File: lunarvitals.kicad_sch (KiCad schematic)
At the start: 26 parts, among them J1 MLX90614, J2 MAX30102, J3 SEN11574, J4 ConductiveCord, U1 NRF52840-DONGLE, U2 BMP280, U3 AP2112K-3.3, U5 MPU-6050

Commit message: PCB layout
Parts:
- removed D2: Green_LED, LED_SMD:LED_0603_1608Metric, symbol Device:LED
- added R8: 4.7k, Resistor_SMD:R_0402_1005Metric, symbol Device:R
- J2: footprint Connector_PinSocket_2.00mm:PinSocket_2x02_P2.00mm_Vertical -> Connector_JST:JST_XA_B04B-XASK-1-A_1x04_P2.50mm_Vertical; symbol Connector_Generic:Conn_02x02_Odd_Even -> Connector_Generic:Conn_01x04; LCSC C46289 -> C491709
- J3, J4: footprint Connector_PinSocket_2.54mm:PinSocket_1x03_P2.54mm_Vertical -> Connector_JST:JST_XA_B03B-XASK-1-A_1x03_P2.50mm_Vertical; LCSC C146690 -> C265055
- R4: value 10k -> 4.7k; LCSC C25744 -> C25900
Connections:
- net +3.3V: now also J2.1 (Pin_1), R8.1; no longer J2.3 (Pin_3)
- net GND: now also J2.4 (Pin_4); no longer J2.1 (Pin_1)
- net I2C1_SCL: now also J2.3 (Pin_3); no longer J2.2 (Pin_2)
- net I2C1_SDA: now also J2.2 (Pin_2); no longer J2.4 (Pin_4)
- net at U5.6 (AUX_DA): now also R4.2
- net at U5.7 (AUX_CL): now also R8.2
- no-connect marks 4 -> 2
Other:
- note added: "LED On Indicator"
- note removed: "LED On Indicator (Red)"
- note removed: "On LED"
- moved on the sheet: J2

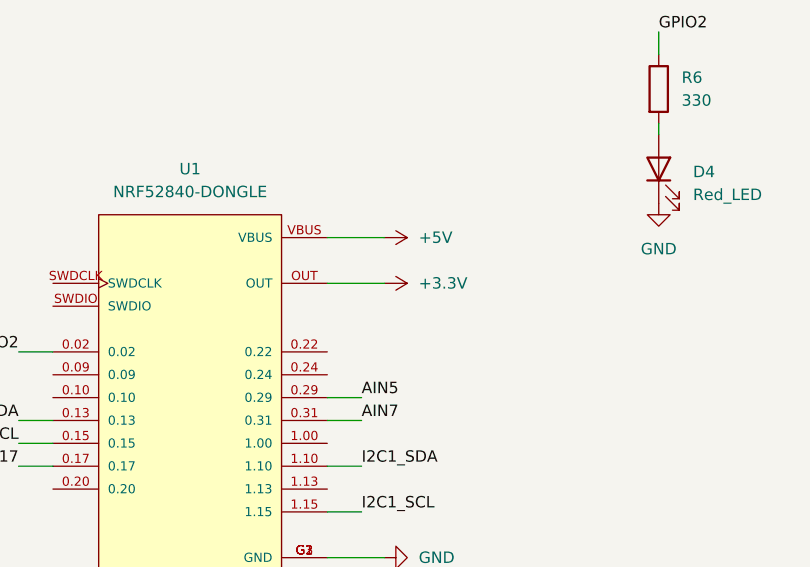
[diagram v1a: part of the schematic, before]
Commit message: removed 2 voltage regulator on same 3.3v connection
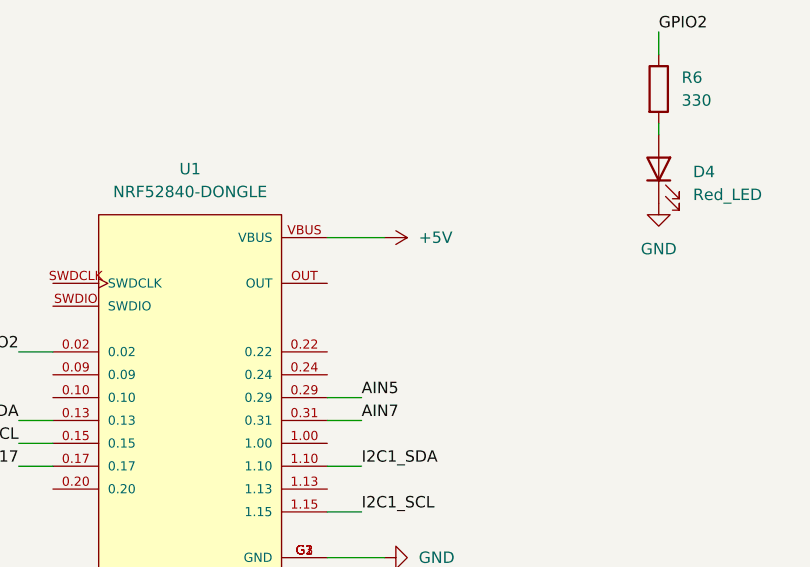
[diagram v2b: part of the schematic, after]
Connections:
- net +3.3V: no longer U1.OUT
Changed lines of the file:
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@@
-	(wire
-		(pts
-			(xy 181.61 60.96) (xy 187.96 60.96)
-		)
-		(stroke
-			(width 0)
-			(type default)
-		)
-	)
 	(wire
 		(pts
@@
 					(unit 1)
 				)
-			)
-		)
-	)
-	(symbol
-		(lib_id "power:+3.3V")
-		(at 187.96 60.96 270)
-		(unit 1)
-		(exclude_from_sim no)
-		(in_bom yes)
-		(on_board yes)
-		(dnp no)
-		(fields_autoplaced yes)
-		(property "Reference" "#PWR03"
-			(at 184.15 60.96 0)
-			(effects
-				(font
-					(size 1.27 1.27)
-				)
-				(hide yes)
-			)
-		)
-		(property "Value" "+3.3V"
-			(at 191.77 60.9599 90)
-			(effects
-				(font
-					(size 1.27 1.27)
-				)
-				(justify left)
-			)
-		)
-		(property "Footprint" ""
-			(at 187.96 60.96 0)
-			(effects
-				(font
-					(size 1.27 1.27)
-				)
-				(hide yes)
-			)
-		)
-		(property "Datasheet" ""
-			(at 187.96 60.96 0)
-			(effects
-				(font
-					(size 1.27 1.27)
-				)
-				(hide yes)
-			)
-		)
-		(property "Description" "Power symbol creates a global label with name \"+3.3V\""
-			(at 187.96 60.96 0)
-			(effects
-				(font
-					(size 1.27 1.27)
-				)
-				(hide yes)
-			)
-		)
-		(pin "1"
-		)
-		(instances
-			(project "lunarvitals"
-				(path "/5743f844-2fd9-4187-922b-f2fa73d8e73e"
-					(reference "#PWR03")
-					(unit 1)
-				)

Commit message: minor fixes to BOM, remove THT parts from BOM
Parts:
- D3: LCSC C9900014381 -> C2288
- J1, J2, J3, J4, U1: now left out of the parts list
- U2: LCSC (none) -> C83291
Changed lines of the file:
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@@
 		(unit 1)
 		(exclude_from_sim no)
-		(in_bom yes)
+		(in_bom no)
 		(on_board yes)
 		(dnp no)
@@
 		(unit 1)
 		(exclude_from_sim no)
-		(in_bom yes)
+		(in_bom no)
 		(on_board yes)
 		(dnp no)
@@
 			)
 		)
+		(property "LCSC" "C83291"
+			(at 234.95 137.16 0)
+			(effects
+				(font
+					(size 1.27 1.27)
+				)
+				(hide yes)
+			)
+		)
 		(pin "6"
 		)
@@
 		(unit 1)
 		(exclude_from_sim no)
-		(in_bom yes)
+		(in_bom no)
 		(on_board yes)
 		(dnp no)
@@
 			)
 		)
-		(property "LCSC" "C9900014381"
+		(property "LCSC" "C2288"
 			(at 238.76 48.26 90)
 			(effects
@@
 		(unit 1)
 		(exclude_from_sim no)
-		(in_bom yes)
+		(in_bom no)
 		(on_board yes)
 		(dnp no)
@@
 		(unit 1)
 		(exclude_from_sim no)
-		(in_bom yes)
-		(on_board yes)
-		(dnp no)
+		(in_bom no)
+		(on_board yes)
+		(dnp no)

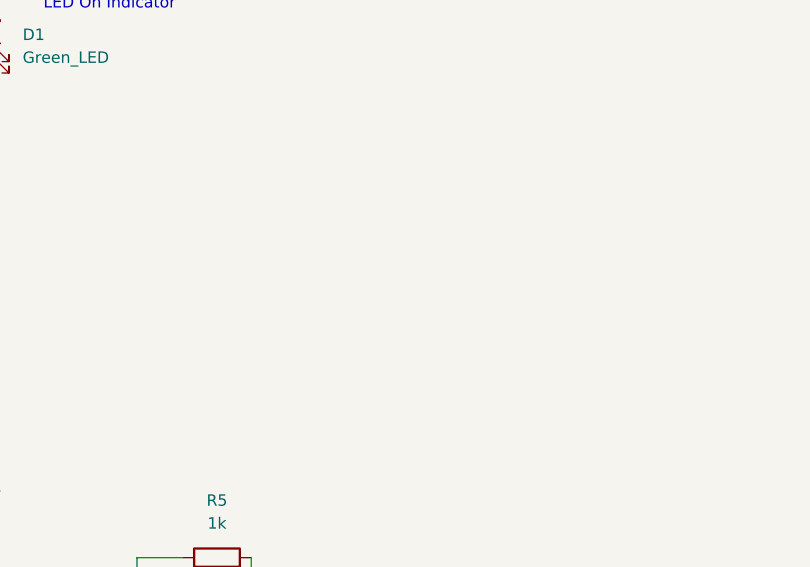
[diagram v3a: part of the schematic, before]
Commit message: add scuffed mounting holes (better than none)
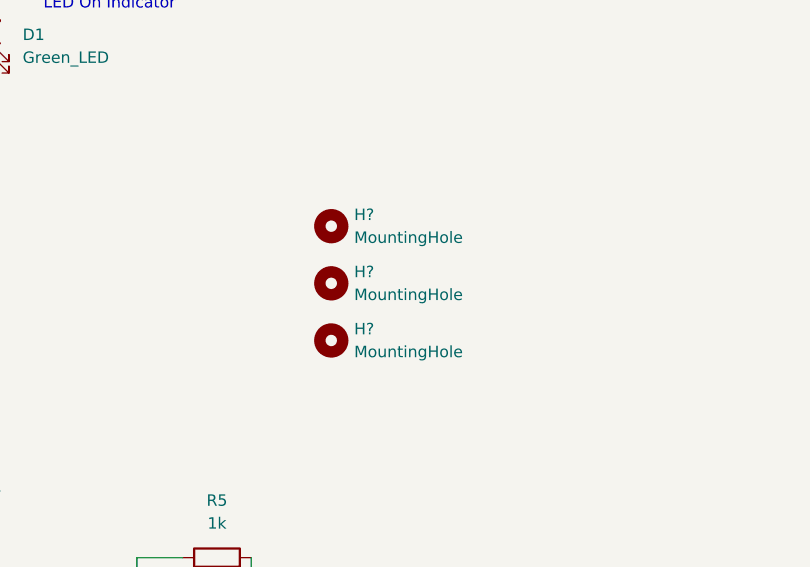
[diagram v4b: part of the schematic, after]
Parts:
- added H? (x3): MountingHole, MountingHole:MountingHole_2.2mm_M2, symbol Mechanical:MountingHole
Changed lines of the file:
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@@
+	)
+	(symbol
+		(lib_id "Mechanical:MountingHole")
+		(at 137.16 130.81 0)
+		(unit 1)
+		(exclude_from_sim yes)
+		(in_bom no)
+		(on_board yes)
+		(dnp no)
+		(fields_autoplaced yes)
+		(property "Reference" "H?"
+			(at 139.7 129.5399 0)
+			(effects
+				(font
+					(size 1.27 1.27)
+				)
+				(justify left)
+			)
+		)
+		(property "Value" "MountingHole"
+			(at 139.7 132.0799 0)
+			(effects
+				(font
+					(size 1.27 1.27)
+				)
+				(justify left)
+			)
+		)
+		(property "Footprint" "MountingHole:MountingHole_2.2mm_M2"
+			(at 137.16 130.81 0)
+			(effects
+				(font
+					(size 1.27 1.27)
+				)
+				(hide yes)
+			)
+		)
+		(property "Datasheet" "~"
+			(at 137.16 130.81 0)
+			(effects
+				(font
+					(size 1.27 1.27)
+				)
+				(hide yes)
+			)
+		)
+		(property "Description" "Mounting Hole without connection"
+			(at 137.16 130.81 0)
+			(effects
+				(font
+					(size 1.27 1.27)
+				)
+				(hide yes)
+			)
+		)
+		(instances
+			(project ""
+				(path "/5743f844-2fd9-4187-922b-f2fa73d8e73e"
+					(reference "H?")
+					(unit 1)
+				)
+			)
+		)
 	)
 	(symbol
@@
 	)
 	(symbol
+		(lib_id "Mechanical:MountingHole")
+		(at 137.16 137.16 0)
+		(unit 1)
+		(exclude_from_sim yes)
+		(in_bom no)
+		(on_board yes)
+		(dnp no)
+		(fields_autoplaced yes)
+		(property "Reference" "H?"
+			(at 139.7 135.8899 0)
+			(effects
+				(font
+					(size 1.27 1.27)
+				)
+				(justify left)
+			)
+		)
+		(property "Value" "MountingHole"
+			(at 139.7 138.4299 0)
+			(effects
+				(font
+					(size 1.27 1.27)
+				)
+				(justify left)
+			)
+		)
+		(property "Footprint" "MountingHole:MountingHole_2.2mm_M2"
+			(at 137.16 137.16 0)
+			(effects
+				(font
+					(size 1.27 1.27)
+				)
+				(hide yes)
+			)
+		)
+		(property "Datasheet" "~"
+			(at 137.16 137.16 0)
+			(effects
+				(font
+					(size 1.27 1.27)
+				)
+				(hide yes)
+			)
+		)
+		(property "Description" "Mounting Hole without connection"
+			(at 137.16 137.16 0)
+			(effects
+				(font
+					(size 1.27 1.27)
+				)
+				(hide yes)
+			)
+		)
+		(instances
+			(project "lunarvitals"
+				(path "/5743f844-2fd9-4187-922b-f2fa73d8e73e"
+					(reference "H?")
+					(unit 1)
+				)
+			)
+		)
+	)
+	(symbol
 		(lib_id "power:GND")
 		(at 237.49 152.4 0)
@@
 					(unit 1)
 				)
+			)
+		)
+	)
+	(symbol
+		(lib_id "Mechanical:MountingHole")
+		(at 137.16 143.51 0)
+		(unit 1)
+		(exclude_from_sim yes)
+		(in_bom no)
+		(on_board yes)
+		(dnp no)
+		(fields_autoplaced yes)
+		(property "Reference" "H?"
+			(at 139.7 142.2399 0)
+			(effects
+				(font
+					(size 1.27 1.27)
+				)
+				(justify left)
+			)
+		)
+		(property "Value" "MountingHole"
+			(at 139.7 144.7799 0)
+			(effects
+				(font
+					(size 1.27 1.27)
+				)
+				(justify left)
+			)
+		)
+		(property "Footprint" "MountingHole:MountingHole_2.2mm_M2"
+			(at 137.16 143.51 0)
+			(effects
+				(font
+					(size 1.27 1.27)
+				)
+				(hide yes)
+			)
+		)
+		(property "Datasheet" "~"
+			(at 137.16 143.51 0)
+			(effects
+				(font
+					(size 1.27 1.27)
+				)
+				(hide yes)
+			)
+		)
+		(property "Description" "Mounting Hole without connection"
+			(at 137.16 143.51 0)
+			(effects
+				(font
+					(size 1.27 1.27)
+				)
+				(hide yes)
+			)
+		)
+		(instances
+			(project "lunarvitals"
+				(path "/5743f844-2fd9-4187-922b-f2fa73d8e73e"
+					(reference "H?")
+					(unit 1)
+				)

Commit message: PCB Updates
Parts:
- removed C7: 0.1uf, Capacitor_SMD:C_0402_1005Metric, symbol Device:C
- removed J1: MLX90614, Connector_PinSocket_2.00mm:PinSocket_2x02_P2.00mm_Vertical, symbol Connector_Generic:Conn_02x02_Odd_Even
- removed J4: ConductiveCord, Connector_JST:JST_XA_B03B-XASK-1-A_1x03_P2.50mm_Vertical, symbol Connector_Generic:Conn_01x03
- removed U5: MPU-6050, Sensor_Motion:InvenSense_QFN-24_4x4mm_P0.5mm, symbol Sensor_Motion:MPU-6050
- added D2: Red_LED, LED_SMD:LED_0603_1608Metric, symbol Device:LED
- added D5: Blue_LED, LED_SMD:LED_0603_1608Metric, symbol Device:LED
- added J1: ConductiveCord, Connector_JST:JST_XH_B2B-XH-AM_1x02_P2.50mm_Vertical, symbol Connector_Generic:Conn_01x02
- added J5: USB_C_Receptacle_PowerOnly_6P, Connector_USB:USB_C_Receptacle_GCT_USB4125-xx-x-0190_6P_TopMnt_Horizontal, symbol Connector:USB_C_Receptacle_PowerOnly_6P
- added J6: Battery, SM02B-SRSS-TB_LF__SN_:SM02B-SRSS-TB_LF__SN_, symbol Connector_Generic:Conn_01x02
- added Q1: FS8205A, FS8205A:SOP65P640X120-8N, symbol FS8205A:FS8205A
- added R10, R11, R13: 1k, Resistor_SMD:R_0402_1005Metric, symbol Device:R
- added R12: 100, Resistor_SMD:R_0402_1005Metric, symbol Device:R
- added R9: 2.4k, Resistor_SMD:R_0402_1005Metric, symbol Device:R
- added U4: TP4056, TP4056:SOP127P600X175-9N, symbol TP4056:TP4056
- added U5: MLX90614ESF-AAA-000-TU, MLX90614ESF-AAA-000-TU:TO254P912H435-4, symbol MLX90614:MLX90614ESF-AAA-000-TU
- added U6: DW01A, Package_TO_SOT_SMD:SOT-23-6, symbol Battery_Management:DW01A
- C2: value 10nf -> 10uf; LCSC C1524 -> C15525
- C3: value 10uf -> 0.1uf; LCSC C15525 -> C1525
- C6: value 2.2nf -> 10uf; LCSC C1531 -> C15525
- J2: value MAX30102 -> MPU6050; footprint Connector_JST:JST_XA_B04B-XASK-1-A_1x04_P2.50mm_Vertical -> Connector_JST:JST_XH_B4B-XH-AM_1x04_P2.50mm_Vertical
- J3: footprint Connector_JST:JST_XA_B03B-XASK-1-A_1x03_P2.50mm_Vertical -> Connector_JST:JST_XH_B3B-XH-AM_1x03_P2.50mm_Vertical
- R4: value 4.7k -> 330; LCSC C25900 -> C12246
- R7: value 330 -> 5.1k; LCSC C12246 -> C25905
- R8: value 4.7k -> 5.1k; LCSC C25900 -> C25905
- gave numbers to parts that had none: 3
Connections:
- net +3.3V: now also U1.OUT, J1.2 (Pin_2), U5.3 (VDD); no longer C5.1, R4.1, R8.1
- net +5V: now also C4.1, D2.2 (A), D5.2 (A), J5.A9 (VBUS), J5.B9 (VBUS), U4.4 (VCC), U4.8 (CE); no longer C1.1, U1.VBUS, U3.1 (VIN), U3.3 (EN)
- net AIN7: now also J1.1 (Pin_1)
- net GND: now also J2.2 (Pin_2), R7.1, R8.2, J5.A12 (GND), J5.B12 (GND), J5.S1 (SHIELD), Q1.6, Q1.7, R13.1, R9.2, U4.1 (TEMP), U4.3 (GND), U4.9 (EP), U5.4 (VSS); no longer C5.2, J2.4 (Pin_4)
- net GPIO17: now also R6.1; no longer R7.1
- net GPIO2: now also R4.1; no longer R6.1
- net I2C0_SCL: now also U5.1 (SCL/VZ)
- net I2C0_SDA: now also U5.2 (SDA/PWM)
- net I2C1_SCL: now also J2.4 (Pin_4); no longer J2.3 (Pin_3)
- net I2C1_SDA: now also J2.3 (Pin_3); no longer J2.2 (Pin_2)
- net BOut+: now reaches C6.1
- net BOut+: now also C1.1, U3.1 (VIN), U3.3 (EN), J6.1 (Pin_1), R12.1, U4.5 (BAT)
- net at R4.2: now also D4.2 (A)
- net at R6.2: now also D3.2 (A); no longer D4.2 (A)
- net at R7.2: now also J5.A5 (CC1); no longer D3.2 (A)
- new net: R9.1, U4.2 (PROG)
- new net: R10.1, U4.6 (~{STDBY})
- new net: D2.1 (K), R10.2
- new net: Q1.1, Q1.8
- new net: Q1.4, U6.1 (OD)
- new net: Q1.5, U6.3 (OC)
- new net: J5.B5 (CC2), R8.1
- new net: R11.1, U4.7 (~{CHRG})
- new net: D5.1 (K), R11.2
- new net: R13.2, U6.2 (CS)
- new net: C5.1, R12.2, U6.5 (VCC)
- new net B-: C5.2, J6.2 (Pin_2), Q1.2, Q1.3, U6.6 (GND)
- no-connect marks 2 -> 1
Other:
- note added: "BOut+ [3.7V-4.2V] gets converted to 3.3V"
- note added: "Charging Monitoring"
- note added: "DIscharging & Protection"
- note added: "FIX CORD VOLTAGE DIVIDER"
- note added: "USB-C"
- note removed: "VCC 5V gets converted to 3.3V"
- moved on the sheet: D1, D3, D4, H1, H2, H3, J2, J3, R3, R5, U1, U2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

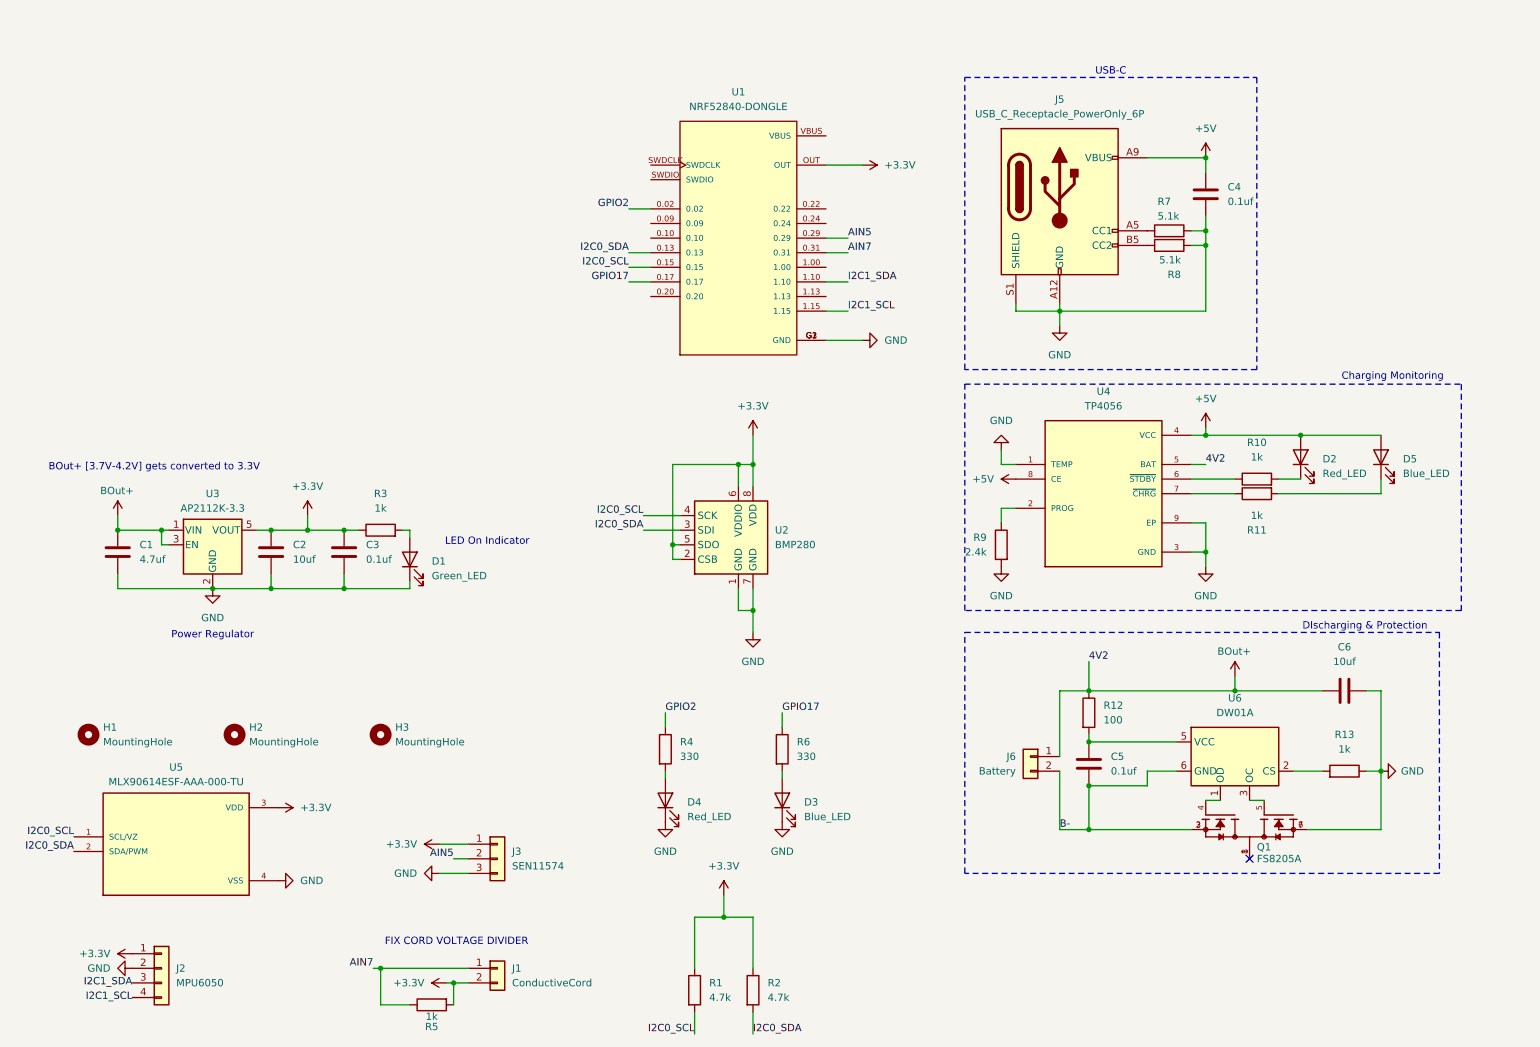
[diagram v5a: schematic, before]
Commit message: pcb updates (logo, conductive cord, charging diodes, layout)
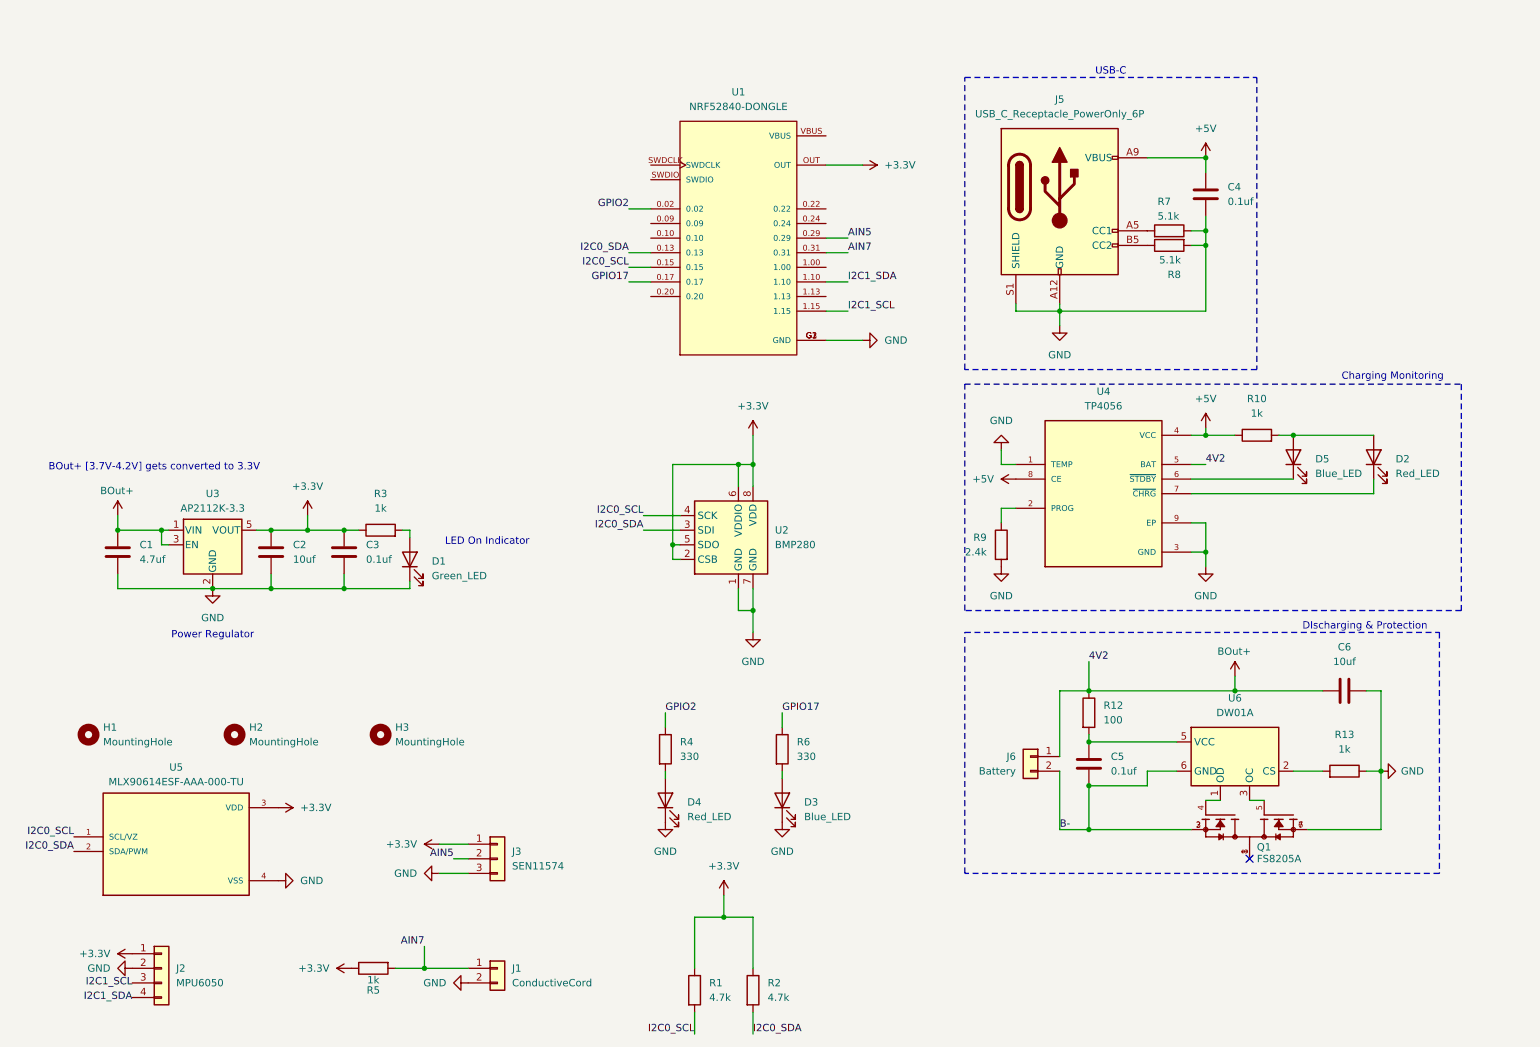
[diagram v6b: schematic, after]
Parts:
- removed R11: 1k, Resistor_SMD:R_0402_1005Metric, symbol Device:R
- J1: footprint Connector_JST:JST_XH_B2B-XH-AM_1x02_P2.50mm_Vertical -> Connector_JST:JST_XH_B2B-XH-A_1x02_P2.50mm_Vertical
- J2: footprint Connector_JST:JST_XH_B4B-XH-AM_1x04_P2.50mm_Vertical -> Connector_JST:JST_XH_B4B-XH-A_1x04_P2.50mm_Vertical
- J3: footprint Connector_JST:JST_XH_B3B-XH-AM_1x03_P2.50mm_Vertical -> Connector_JST:JST_XH_B3B-XH-A_1x03_P2.50mm_Vertical
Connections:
- net +3.3V: now also R5.1; no longer J1.2 (Pin_2), R5.2
- net +5V: now also R10.1; no longer D2.2 (A), D5.2 (A)
- net AIN7: now also R5.2; no longer R5.1
- net GND: now also J1.2 (Pin_2)
- net I2C1_SCL: now also J2.3 (Pin_3); no longer J2.4 (Pin_4)
- net I2C1_SDA: now also J2.4 (Pin_4); no longer J2.3 (Pin_3)
- net at U4.6 (~{STDBY}): now also D5.1 (K); no longer R10.1
- net at R10.2: now also D2.2 (A), D5.2 (A); no longer D2.1 (K)
- net at U4.7 (~{CHRG}): now also D2.1 (K)
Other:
- note removed: "FIX CORD VOLTAGE DIVIDER"
- moved on the sheet: D2, D5, R10, R5
